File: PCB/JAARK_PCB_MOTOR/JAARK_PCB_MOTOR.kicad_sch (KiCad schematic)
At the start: 68 parts, among them IC1 TPS564242DRLR, IC10 DRV8231DDAR, IC2 PJA3404_R1_00001, IC3 PJA3404_R1_00001, IC4 HIP4080AIBZT, IC5 PJA3404_R1_00001, IC6 PJA3404_R1_00001, IC7 PJA3404_R1_00001, IC8 PJA3404_R1_00001, IC9 DRV8231DDAR, J1 Battery Terminal, J2 Morpho_x2_SSW-119-01-T-D, Q1 SSM3J334RLF, Q2 SSM3J334RLF, Q3 FMMT619TA, Q4 FMMT619TA, Q5 FMMT619TA, Q6 SSM3J334RLF, Q7 FMMT619TA, U1 4A

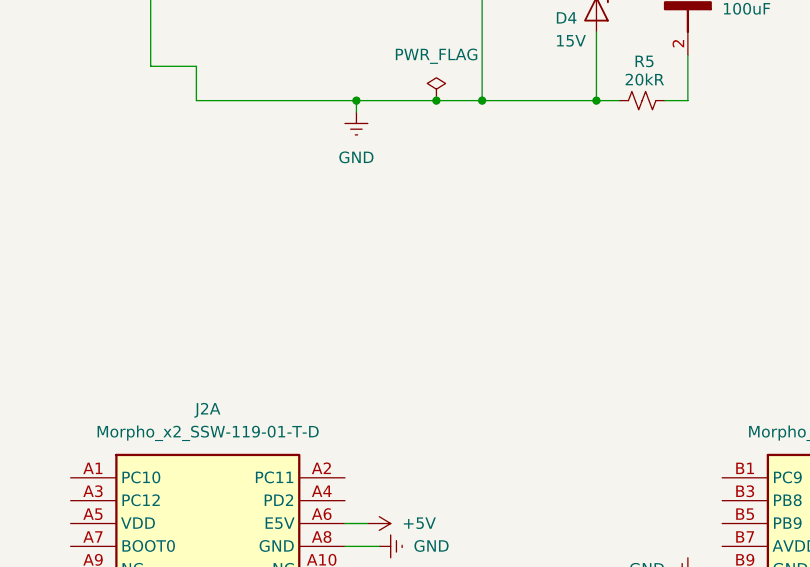
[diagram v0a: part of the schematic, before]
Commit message: "Added heat sink"
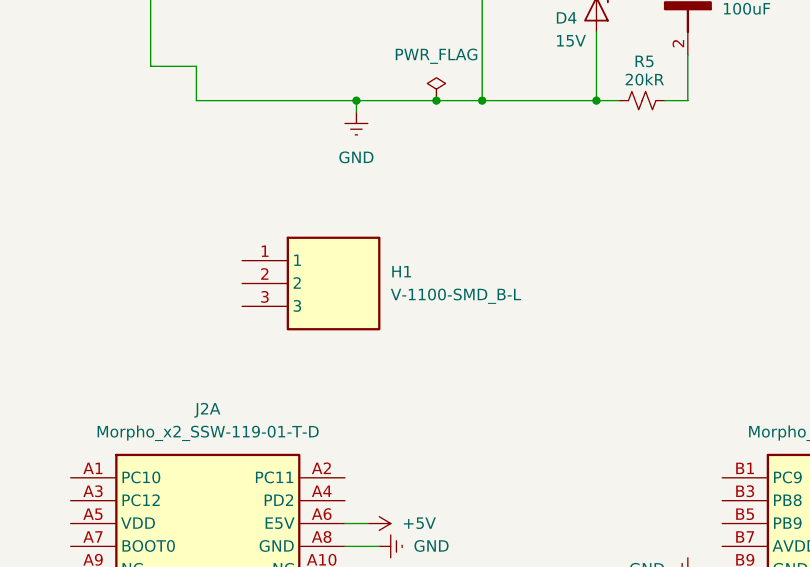
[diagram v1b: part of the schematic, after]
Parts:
- added H1: V-1100-SMD_B-L, V1100SMDBL, symbol JAARK_lib:V-1100-SMD_B-L
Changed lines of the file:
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@@
+	)
+	(symbol
+		(lib_id "JAARK_lib:V-1100-SMD_B-L")
+		(at 46.99 76.2 0)
+		(unit 1)
+		(exclude_from_sim no)
+		(in_bom yes)
+		(on_board yes)
+		(dnp no)
+		(fields_autoplaced yes)
+		(property "Reference" "H1"
+			(at 63.5 77.4699 0)
+			(effects
+				(font
+					(size 1.27 1.27)
+				)
+				(justify left)
+			)
+		)
+		(property "Value" "V-1100-SMD_B-L"
+			(at 63.5 80.0099 0)
+			(effects
+				(font
+					(size 1.27 1.27)
+				)
+				(justify left)
+			)
+		)
+		(property "Footprint" "V1100SMDBL"
+			(at 63.5 171.12 0)
+			(effects
+				(font
+					(size 1.27 1.27)
+				)
+				(justify left top)
+				(hide yes)
+			)
+		)
+		(property "Datasheet" "https://www.digikey.com/en/products/detail/assmann-wsw-components/V-1100-SMD-B-L/3511509?msockid=3e3afa68a50969ca3057ef1ca4c9684b"
+			(at 63.5 271.12 0)
+			(effects
+				(font
+					(size 1.27 1.27)
+				)
+				(justify left top)
+				(hide yes)
+			)
+		)
+		(property "Description" "Heat Sink TO-252 (DPak) Copper Top Mount"
+			(at 46.99 76.2 0)
+			(effects
+				(font
+					(size 1.27 1.27)
+				)
+				(hide yes)
+			)
+		)
+		(property "Height" "10.206"
+			(at 63.5 471.12 0)
+			(effects
+				(font
+					(size 1.27 1.27)
+				)
+				(justify left top)
+				(hide yes)
+			)
+		)
+		(property "Manufacturer_Name" "ASSMANN WSW components GmbH"
+			(at 63.5 571.12 0)
+			(effects
+				(font
+					(size 1.27 1.27)
+				)
+				(justify left top)
+				(hide yes)
+			)
+		)
+		(property "Manufacturer_Part_Number" "V-1100-SMD/B-L"
+			(at 63.5 671.12 0)
+			(effects
+				(font
+					(size 1.27 1.27)
+				)
+				(justify left top)
+				(hide yes)
+			)
+		)
+		(property "Mouser Part Number" ""
+			(at 63.5 771.12 0)
+			(effects
+				(font
+					(size 1.27 1.27)
+				)
+				(justify left top)
+				(hide yes)
+			)
+		)
+		(property "Mouser Price/Stock" ""
+			(at 63.5 871.12 0)
+			(effects
+				(font
+					(size 1.27 1.27)
+				)
+				(justify left top)
+				(hide yes)
+			)
+		)
+		(property "Arrow Part Number" "V-1100-SMD/B-L"
+			(at 63.5 971.12 0)
+			(effects
+				(font
+					(size 1.27 1.27)
+				)
+				(justify left top)
+				(hide yes)
+			)
+		)
+		(property "Arrow Price/Stock" "https://www.arrow.com/en/products/v-1100-smdb-l/assmann-wsw-components-inc?utm_currency=USD&region=nac"
+			(at 63.5 1071.12 0)
+			(effects
+				(font
+					(size 1.27 1.27)
+				)
+				(justify left top)
+				(hide yes)
+			)
+		)
+		(pin "1"
+		)
+		(pin "3"
+		)
+		(pin "2"
+		)
+		(instances
+			(project ""
+				(path "/855a2ad7-0ca6-4188-a452-4c1fc0d76ca5"
+					(reference "H1")
+					(unit 1)
+				)
+			)
+		)
 	)
 	(symbol

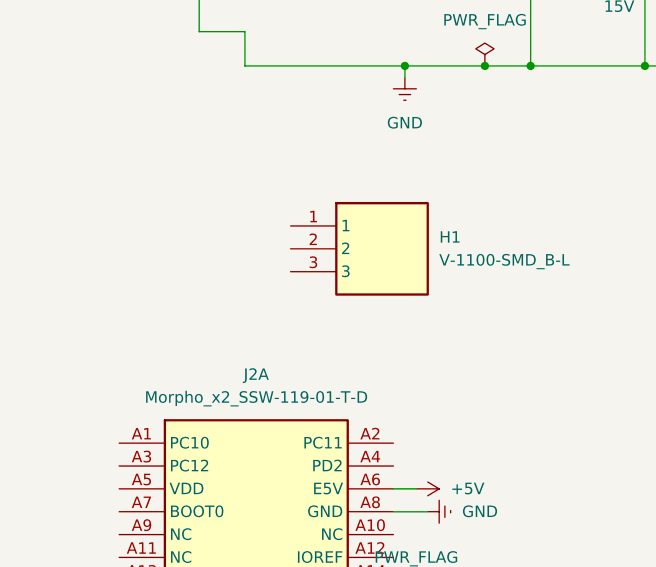
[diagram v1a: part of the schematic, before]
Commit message: Added heat sink to PCB file and adjusted footprint
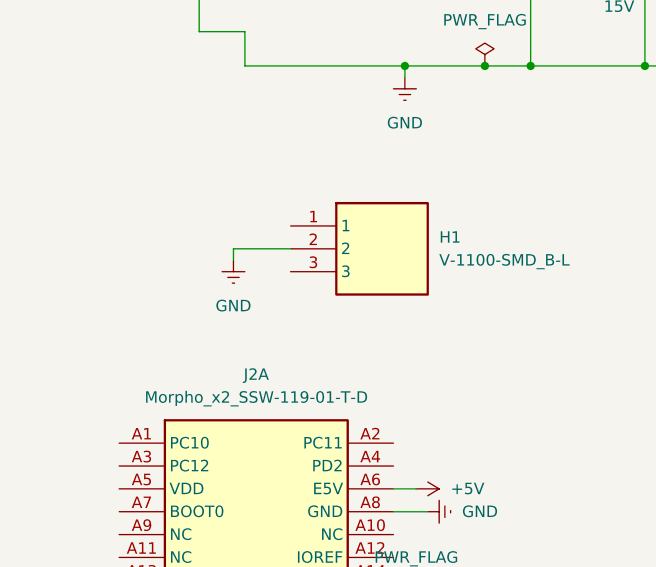
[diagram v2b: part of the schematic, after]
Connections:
- net GND: now also H1.2
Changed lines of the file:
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@@
 	(wire
 		(pts
+			(xy 46.99 78.74) (xy 40.64 78.74)
+		)
+		(stroke
+			(width 0)
+			(type default)
+		)
+	)
+	(wire
+		(pts
 			(xy 499.11 81.28) (xy 514.35 81.28)
 		)
@@
 	(wire
 		(pts
+			(xy 40.64 78.74) (xy 40.64 80.01)
+		)
+		(stroke
+			(width 0)
+			(type default)
+		)
+	)
+	(wire
+		(pts
 			(xy 147.32 57.15) (xy 148.59 57.15)
 		)
@@
 					(unit 1)
 				)
+			)
+		)
+	)
+	(symbol
+		(lib_id "power:GNDREF")
+		(at 40.64 80.01 0)
+		(unit 1)
+		(exclude_from_sim no)
+		(in_bom yes)
+		(on_board yes)
+		(dnp no)
+		(fields_autoplaced yes)
+		(property "Reference" "#PWR048"
+			(at 40.64 86.36 0)
+			(effects
+				(font
+					(size 1.27 1.27)
+				)
+				(hide yes)
+			)
+		)
+		(property "Value" "GND"
+			(at 40.64 85.09 0)
+			(effects
+				(font
+					(size 1.27 1.27)
+				)
+			)
+		)
+		(property "Footprint" ""
+			(at 40.64 80.01 0)
+			(effects
+				(font
+					(size 1.27 1.27)
+				)
+				(hide yes)
+			)
+		)
+		(property "Datasheet" ""
+			(at 40.64 80.01 0)
+			(effects
+				(font
+					(size 1.27 1.27)
+				)
+				(hide yes)
+			)
+		)
+		(property "Description" "Power symbol creates a global label with name \"GNDREF\" , reference supply ground"
+			(at 40.64 80.01 0)
+			(effects
+				(font
+					(size 1.27 1.27)
+				)
+				(hide yes)
+			)
+		)
+		(pin "1"
+		)
+		(instances
+			(project "JAARK_PCB_MOTOR"
+				(path "/855a2ad7-0ca6-4188-a452-4c1fc0d76ca5"
+					(reference "#PWR048")
+					(unit 1)
+				)

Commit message: More work on PCB, removed heatsink and then added mounting holes again
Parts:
- removed C10, C9: 100uF, JAARK_lib:CAPC3216X180N, symbol Device:C_Small
- removed C11: 33uF, JAARK_lib:CAPC3216X180N, symbol Device:C_Small
- removed D10, D11, D2, D3, D8, D9: S2JTR, Diode_SMD:D_SMB, symbol Diode:S2JTR
- removed H1: V-1100-SMD_B-L, V1100SMDBL, symbol JAARK_lib:V-1100-SMD_B-L
- removed IC2, IC3, IC5, IC6, IC7, IC8: PJA3404_R1_00001, SOT95P240X110-3N, symbol JAARK_lib:SSM3J334R,LF
- removed IC4: HIP4080AIBZT, SOIC127P1032X265-20N, symbol JAARK_lib:HIP4080AIBZT
- removed J3, J4: ~, JAARK_lib:1984617, symbol SSys_Parts:1984617
- removed Q2, Q6: SSM3J334RLF, 2SC2712GRLF, symbol JAARK_lib:SSM3J334R,LF
- removed Q3, Q4, Q5, Q7: FMMT619TA, SOT95P237X112-3N, symbol JAARK_lib:FMMT619TA
- removed R14, R16, R21, R22: 260R, RESC2012X60N, symbol Device:R_Small_US
- removed R15, R17, R18, R7: 5kR, RESC2012X50N, symbol Device:R_Small_US
- removed R19, R20: 10kR, RESC2012X60N, symbol Device:R_Small_US
- removed R6, R8, R9: 20kR, RESC2012X50N, symbol Device:R_Small_US
- removed V2: 3.3, symbol Simulation_SPICE:VDC
- removed V3: 0, symbol Simulation_SPICE:VDC
- J2: now left out of the parts list
- U1: symbol JAARK_lib:Fuse -> JAARK_lib:3586TR
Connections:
- net GND: now also J2.B20 (GND), J2.B32 (AGND)
- net at J1.2: now also U1.2; no longer U1.1
- net at Q1.3 (D): now also U1.1; no longer U1.2
- no-connect marks 0 -> 64
